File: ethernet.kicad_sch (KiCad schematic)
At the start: 19 parts, among them J6 J1B1211CCD, U1 MX6UL-VM, U18 DP83825, U25 TPD4EUSB30

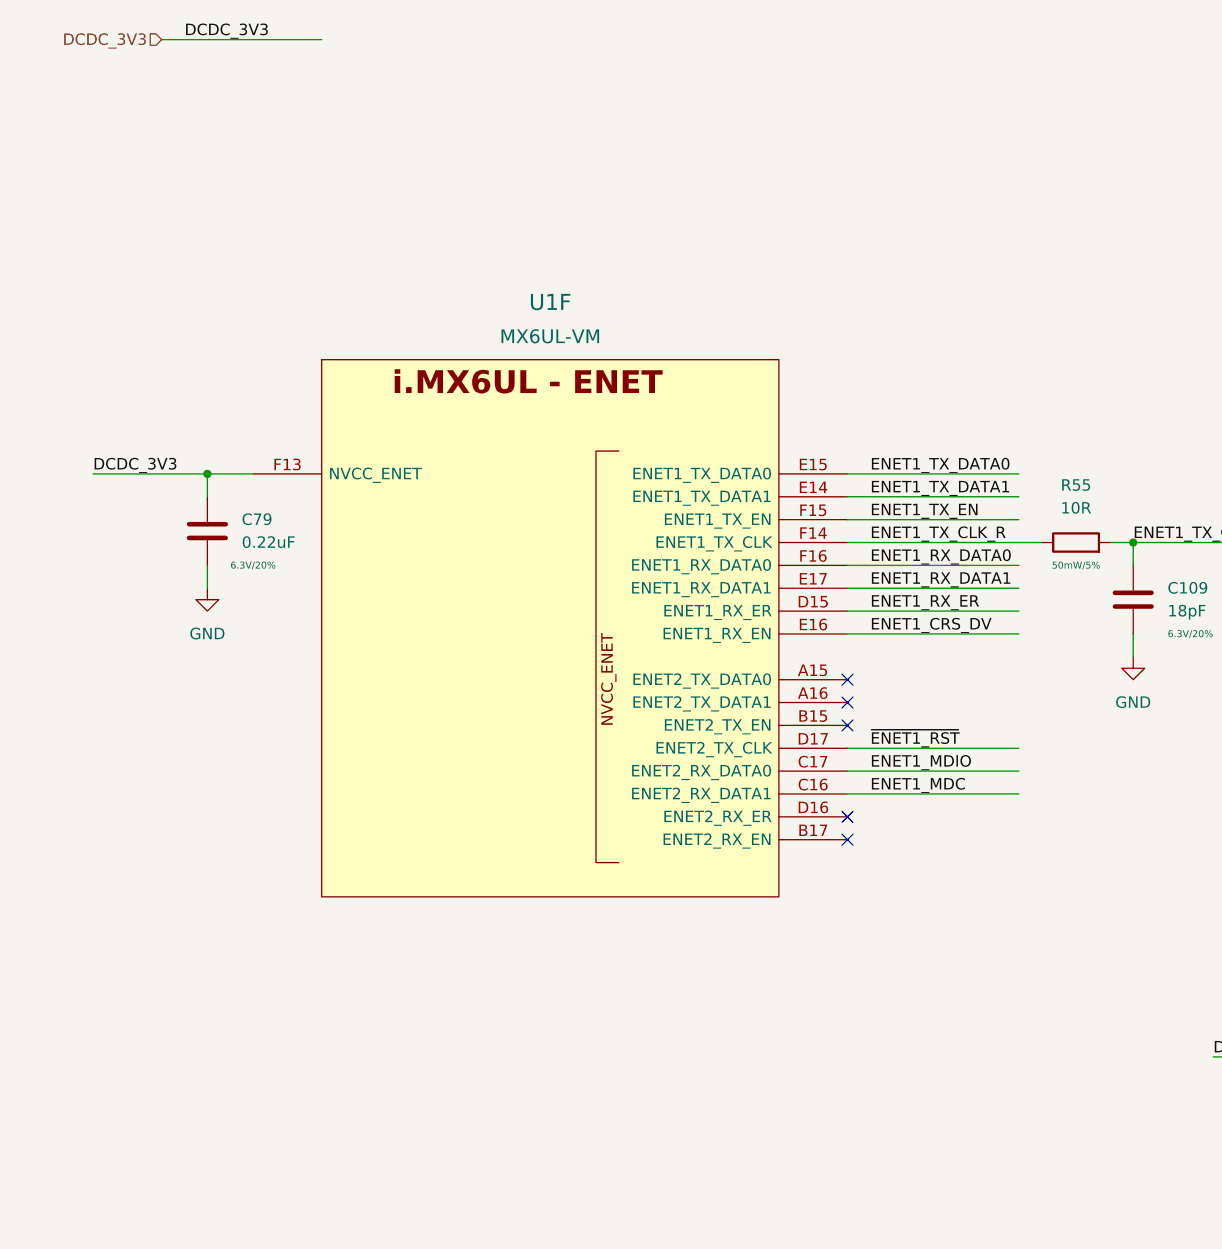
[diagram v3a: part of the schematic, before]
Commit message: lots of routing, ddr length matching done
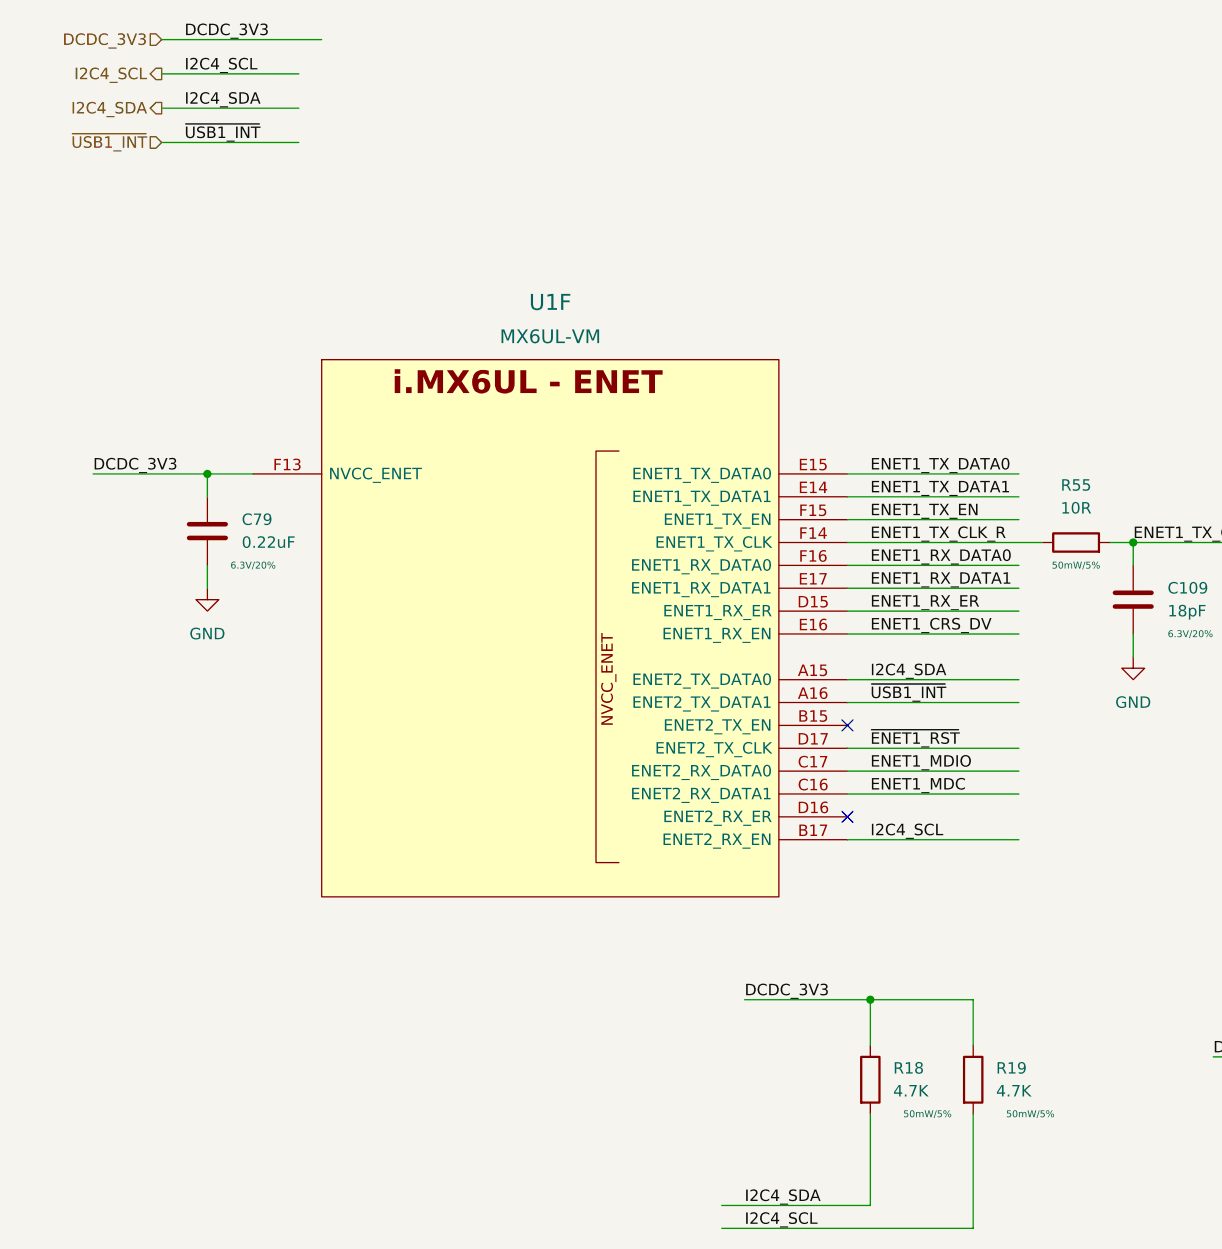
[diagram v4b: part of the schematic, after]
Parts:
- added R18, R19: 4.7K, Resistor_SMD:R_0402_1005Metric, symbol Device:R
- C79: footprint Capacitor_SMD:C_0402_1005Metric -> Capacitor_SMD:C_0201_0603Metric
- J6: footprint imx6ull-sbc:J1B1211CCD -> qsbc-zero:J1B1211CCD; symbol imx6ull-sbc:J1B1211CCD -> qsbc-zero:J1B1211CCD
- U1: footprint imx6ull-sbc:SOT1534-2 -> qsbc-zero:SOT1534-2; symbol imx6ull-sbc:MX6UL-VM -> qsbc-zero:MX6UL-VM
- U18: footprint imx6ull-sbc:XCVR_DP83825IRMQR -> qsbc-zero:XCVR_DP83825IRMQR; symbol imx6ull-sbc:DP83825 -> qsbc-zero:DP83825
- U25: symbol imx6ull-sbc:TPD4EUSB30 -> qsbc-zero:TPD4EUSB30
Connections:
- net DCDC_3V3: now also R18.1, R19.1
- net I2C4_SDA: now reaches U1.A15 (ENET2_TX_DATA0)
- net I2C4_SDA: now also R18.2
- net ~{USB1_INT}: now reaches U1.A16 (ENET2_TX_DATA1)
- net I2C4_SCL: now reaches U1.B17 (ENET2_RX_EN)
- net I2C4_SCL: now also R19.2
- no-connect marks 8 -> 5

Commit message: more pcb work, bom work
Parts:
- C109: DigiKey_PN (none) -> 311-1415-1-ND; MPN (none) -> CC0402JRNPO9BN180; Rating 6.3V/20% -> 50V/5%
- C110, C111: DigiKey_PN (none) -> 490-GRM155R60J106ME05DCT-ND; MPN (none) -> GRM155R60J106ME05D
- C112, C113: DigiKey_PN (none) -> 490-13409-1-ND; MPN (none) -> GCM155C71A105KE38D; Rating 6.3V/20% -> 10V/20%
- C122, C123: DigiKey_PN (none) -> 490-14603-1-ND; MPN (none) -> GRM155R71E104KE14J
- C79: DigiKey_PN (none) -> 490-10392-1-ND; MPN (none) -> GRM033C80J224KE90D
- J6: DigiKey_PN (none) -> 1278-1052-ND; MPN (none) -> J1B1211CCD
- R114: DigiKey_PN (none) -> 311-2.2KJRCT-ND; MPN (none) -> RC0402JR-072K2L
- R115: DigiKey_PN (none) -> 311-6.49KLRCT-ND; MPN (none) -> RC0402FR-076K49L
- R131, R132: DigiKey_PN (none) -> 311-2.49KLRCT-ND; MPN (none) -> RC0402FR-072K49L; Rating 50mW/5% -> 50mW/1%
- R133, R134: DigiKey_PN (none) -> 311-1.0KJRCT-ND; MPN (none) -> RC0402JR-071KL
- R18, R19: DigiKey_PN (none) -> 311-4.7KJRCT-ND; MPN (none) -> RC0402JR-074K7L
- R55: DigiKey_PN (none) -> 311-10JRCT-ND; MPN (none) -> RC0402JR-0710RL
- U1: DigiKey_PN (none) -> 568-14995-ND; MPN (none) -> MCIMX6Y2DVM09AB
- U18: DigiKey_PN (none) -> 296-DP83825IRMQRCT-ND; MPN (none) -> DP83825IRMQR
- U25: DigiKey_PN (none) -> 296-28063-1-ND; MPN (none) -> TPD4EUSB30DQAR
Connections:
- net GND: now also U18.26 (EPAD), U18.27 (EPAD), U18.28 (EPAD), U18.29 (EPAD), U18.30 (EPAD)
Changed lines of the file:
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@@
       (effects (font (size 1.524 1.524)))
+    )
+    (property "DigiKey_PN" "568-14995-ND" (id 4) (at 71.12 54.61 0)
+      (effects (font (size 1.27 1.27)) hide)
+    )
+    (property "MPN" "MCIMX6Y2DVM09AB" (id 5) (at 71.12 54.61 0)
+      (effects (font (size 1.27 1.27)) hide)
     )
     (pin "A15")
@@
       (effects (font (size 1.27 1.27)) hide)
     )
+    (property "DigiKey_PN" "296-DP83825IRMQRCT-ND" (id 4) (at 212.09 88.9 0)
+      (effects (font (size 1.27 1.27)) hide)
+    )
+    (property "MPN" "DP83825IRMQR" (id 5) (at 212.09 88.9 0)
+      (effects (font (size 1.27 1.27)) hide)
+    )
     (pin "1")
     (pin "10")
@@
     (pin "9")
     (pin "25")
+    (pin "26")
+    (pin "27")
+    (pin "28")
+    (pin "29")
+    (pin "30")
   )
   (symbol (lib_id "power:GND") (at 321.31 116.84 0) (unit 1)
@@
       (effects (font (size 0.762 0.762)))
     )
+    (property "DigiKey_PN" "311-1.0KJRCT-ND" (id 5) (at 269.24 82.55 0)
+      (effects (font (size 1.27 1.27)) hide)
+    )
+    (property "MPN" "RC0402JR-071KL" (id 6) (at 269.24 82.55 0)
+      (effects (font (size 1.27 1.27)) hide)
+    )
     (pin "1")
     (pin "2")
@@
     )
     (property "Datasheet" "http://www.ti.com/lit/ds/symlink/tpd2eusb30a.pdf" (id 3) (at 280.67 129.54 0)
+      (effects (font (size 1.27 1.27)) hide)
+    )
+    (property "DigiKey_PN" "296-28063-1-ND" (id 4) (at 280.67 129.54 0)
+      (effects (font (size 1.27 1.27)) hide)
+    )
+    (property "MPN" "TPD4EUSB30DQAR" (id 5) (at 280.67 129.54 0)
       (effects (font (size 1.27 1.27)) hide)
     )
@@
       (effects (font (size 0.762 0.762)))
     )
+    (property "DigiKey_PN" "490-GRM155R60J106ME05DCT-ND" (id 5) (at 220.98 52.07 0)
+      (effects (font (size 1.27 1.27)) hide)
+    )
+    (property "MPN" "GRM155R60J106ME05D" (id 6) (at 220.98 52.07 0)
+      (effects (font (size 1.27 1.27)) hide)
+    )
     (pin "1")
     (pin "2")
@@
       (effects (font (size 1.27 1.27)) hide)
     )
-    (property "Rating" "50mW/5%" (id 4) (at 201.93 149.86 90)
-      (effects (font (size 0.762 0.762)))
+    (property "Rating" "50mW/1%" (id 4) (at 201.93 149.86 90)
+      (effects (font (size 0.762 0.762)))
+    )
+    (property "DigiKey_PN" "311-2.49KLRCT-ND" (id 5) (at 201.93 147.32 0)
+      (effects (font (size 1.27 1.27)) hide)
+    )
+    (property "MPN" "RC0402FR-072K49L" (id 6) (at 201.93 147.32 0)
+      (effects (font (size 1.27 1.27)) hide)
     )
     (pin "1")
@@
       (effects (font (size 1.27 1.27)) hide)
     )
-    (property "Rating" "6.3V/20%" (id 4) (at 265.43 55.88 0)
-      (effects (font (size 0.762 0.762)))
+    (property "Rating" "10V/20%" (id 4) (at 265.43 55.88 0)
+      (effects (font (size 0.762 0.762)))
+    )
+    (property "DigiKey_PN" "490-13409-1-ND" (id 5) (at 259.08 52.07 0)
+      (effects (font (size 1.27 1.27)) hide)
+    )
+    (property "MPN" "GCM155C71A105KE38D" (id 6) (at 259.08 52.07 0)
+      (effects (font (size 1.27 1.27)) hide)
     )
     (pin "1")
@@
       (effects (font (size 0.762 0.762)))
     )
+    (property "DigiKey_PN" "311-4.7KJRCT-ND" (id 5) (at 106.68 134.62 0)
+      (effects (font (size 1.27 1.27)) hide)
+    )
+    (property "MPN" "RC0402JR-074K7L" (id 6) (at 106.68 134.62 0)
+      (effects (font (size 1.27 1.27)) hide)
+    )
     (pin "1")
     (pin "2")
@@
       (effects (font (size 0.762 0.762)))
     )
+    (property "DigiKey_PN" "490-14603-1-ND" (id 5) (at 298.45 97.79 0)
+      (effects (font (size 1.27 1.27)) hide)
+    )
+    (property "MPN" "GRM155R71E104KE14J" (id 6) (at 298.45 97.79 0)
+      (effects (font (size 1.27 1.27)) hide)
+    )
     (pin "1")
     (pin "2")
@@
     (property "Rating" "25V/20%" (id 4) (at 317.5 101.6 0)
       (effects (font (size 0.762 0.762)))
+    )
+    (property "DigiKey_PN" "490-14603-1-ND" (id 5) (at 311.15 97.79 0)
+      (effects (font (size 1.27 1.27)) hide)
+    )
+    (property "MPN" "GRM155R71E104KE14J" (id 6) (at 311.15 97.79 0)
+      (effects (font (size 1.27 1.27)) hide)
     )
     (pin "1")
@@
       (effects (font (size 0.762 0.762)))
     )
+    (property "DigiKey_PN" "311-6.49KLRCT-ND" (id 5) (at 256.54 102.87 0)
+      (effects (font (size 1.27 1.27)) hide)
+    )
+    (property "MPN" "RC0402FR-076K49L" (id 6) (at 256.54 102.87 0)
+      (effects (font (size 1.27 1.27)) hide)
+    )
     (pin "1")
     (pin "2")
@@
       (effects (font (size 1.27 1.27)) hide)
     )
-    (property "Rating" "6.3V/20%" (id 4) (at 252.73 55.88 0)
-      (effects (font (size 0.762 0.762)))
+    (property "Rating" "10V/20%" (id 4) (at 252.73 55.88 0)
+      (effects (font (size 0.762 0.762)))
+    )
+    (property "DigiKey_PN" "490-13409-1-ND" (id 5) (at 246.38 52.07 0)
+      (effects (font (size 1.27 1.27)) hide)
+    )
+    (property "MPN" "GCM155C71A105KE38D" (id 6) (at 246.38 52.07 0)
+      (effects (font (size 1.27 1.27)) hide)
     )
     (pin "1")
@@
       (effects (font (size 1.27 1.27)) hide)
     )
-    (property "Rating" "6.3V/20%" (id 4) (at 142.24 85.09 0)
-      (effects (font (size 0.762 0.762)))
+    (property "Rating" "50V/5%" (id 4) (at 142.24 85.09 0)
+      (effects (font (size 0.762 0.762)))
+    )
+    (property "DigiKey_PN" "311-1415-1-ND" (id 5) (at 135.89 81.28 0)
+      (effects (font (size 1.27 1.27)) hide)
+    )
+    (property "MPN" "CC0402JRNPO9BN180" (id 6) (at 135.89 81.28 0)
+      (effects (font (size 1.27 1.27)) hide)
     )
     (pin "1")
@@
       (effects (font (size 1.27 1.27)) hide)
     )
-    (property "Rating" "50mW/5%" (id 4) (at 166.37 149.86 90)
-      (effects (font (size 0.762 0.762)))
+    (property "Rating" "50mW/1%" (id 4) (at 166.37 149.86 90)
+      (effects (font (size 0.762 0.762)))
+    )
+    (property "DigiKey_PN" "311-2.49KLRCT-ND" (id 5) (at 166.37 147.32 0)
+      (effects (font (size 1.27 1.27)) hide)
+    )
+    (property "MPN" "RC0402FR-072K49L" (id 6) (at 166.37 147.32 0)
+      (effects (font (size 1.27 1.27)) hide)
     )
     (pin "1")
@@
     (property "Datasheet" "http://wizwiki.net/wiki/lib/exe/fetch.php?media=products:wiz550web:wiz550webds_kr:j1b1211ccd.pdf" (id 3) (at 346.71 93.98 0)
       (effects (font (size 1.27 1.27)) (justify left bottom) hide)
+    )
+    (property "DigiKey_PN" "1278-1052-ND" (id 4) (at 346.71 93.98 0)
+      (effects (font (size 1.27 1.27)) hide)
+    )
+    (property "MPN" "J1B1211CCD" (id 5) (at 346.71 93.98 0)
+      (effects (font (size 1.27 1.27)) hide)
     )
     (pin "1")
@@
       (effects (font (size 0.762 0.762)))
     )
+    (property "DigiKey_PN" "311-1.0KJRCT-ND" (id 5) (at 269.24 93.98 0)
+      (effects (font (size 1.27 1.27)) hide)
+    )
+    (property "MPN" "RC0402JR-071KL" (id 6) (at 269.24 93.98 0)
+      (effects (font (size 1.27 1.27)) hide)
+    )
     (pin "1")
     (pin "2")
@@
       (effects (font (size 0.762 0.762)))
     )
+    (property "DigiKey_PN" "311-4.7KJRCT-ND" (id 5) (at 118.11 134.62 0)
+      (effects (font (size 1.27 1.27)) hide)
+    )
+    (property "MPN" "RC0402JR-074K7L" (id 6) (at 118.11 134.62 0)
+      (effects (font (size 1.27 1.27)) hide)
+    )
     (pin "1")
     (pin "2")
@@
     (property "Rating" "6.3V/20%" (id 4) (at 240.03 55.88 0)
       (effects (font (size 0.762 0.762)))
+    )
+    (property "DigiKey_PN" "490-GRM155R60J106ME05DCT-ND" (id 5) (at 233.68 52.07 0)
+      (effects (font (size 1.27 1.27)) hide)
+    )
+    (property "MPN" "GRM155R60J106ME05D" (id 6) (at 233.68 52.07 0)
+      (effects (font (size 1.27 1.27)) hide)
     )
     (pin "1")
@@
       (effects (font (size 0.762 0.762)))
     )
+    (property "DigiKey_PN" "311-2.2KJRCT-ND" (id 5) (at 162.56 66.04 0)
+      (effects (font (size 1.27 1.27)) hide)
+    )
+    (property "MPN" "RC0402JR-072K2L" (id 6) (at 162.56 66.04 0)
+      (effects (font (size 1.27 1.27)) hide)
+    )
     (pin "1")
     (pin "2")
@@
     (property "Rating" "6.3V/20%" (id 4) (at 38.1 77.47 0)
       (effects (font (size 0.762 0.762)))
+    )
+    (property "DigiKey_PN" "490-10392-1-ND" (id 5) (at 33.02 73.66 0)
+      (effects (font (size 1.27 1.27)) hide)
+    )
+    (property "MPN" "GRM033C80J224KE90D" (id 6) (at 33.02 73.66 0)
+      (effects (font (size 1.27 1.27)) hide)
     )
     (pin "1")
@@
       (effects (font (size 0.762 0.762)))
     )
-    (pin "1")
+    (property "DigiKey_PN" "311-10JRCT-ND" (id 5) (at 129.54 74.93 0)
+      (effects (font (size 1.27 1.27)) hide)
+    )
+    (property "MPN" "RC0402JR-0710RL" (id 6) (at 129.54 74.93 0)
+      (effects (font (size 1.27 1.27)) hide)
+    )
+    (pin "1")
